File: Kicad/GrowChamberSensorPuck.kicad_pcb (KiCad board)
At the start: 2 copper layers, 11 parts, among them P1 CONN_01X07, U1 Si7006, U2 CCS811

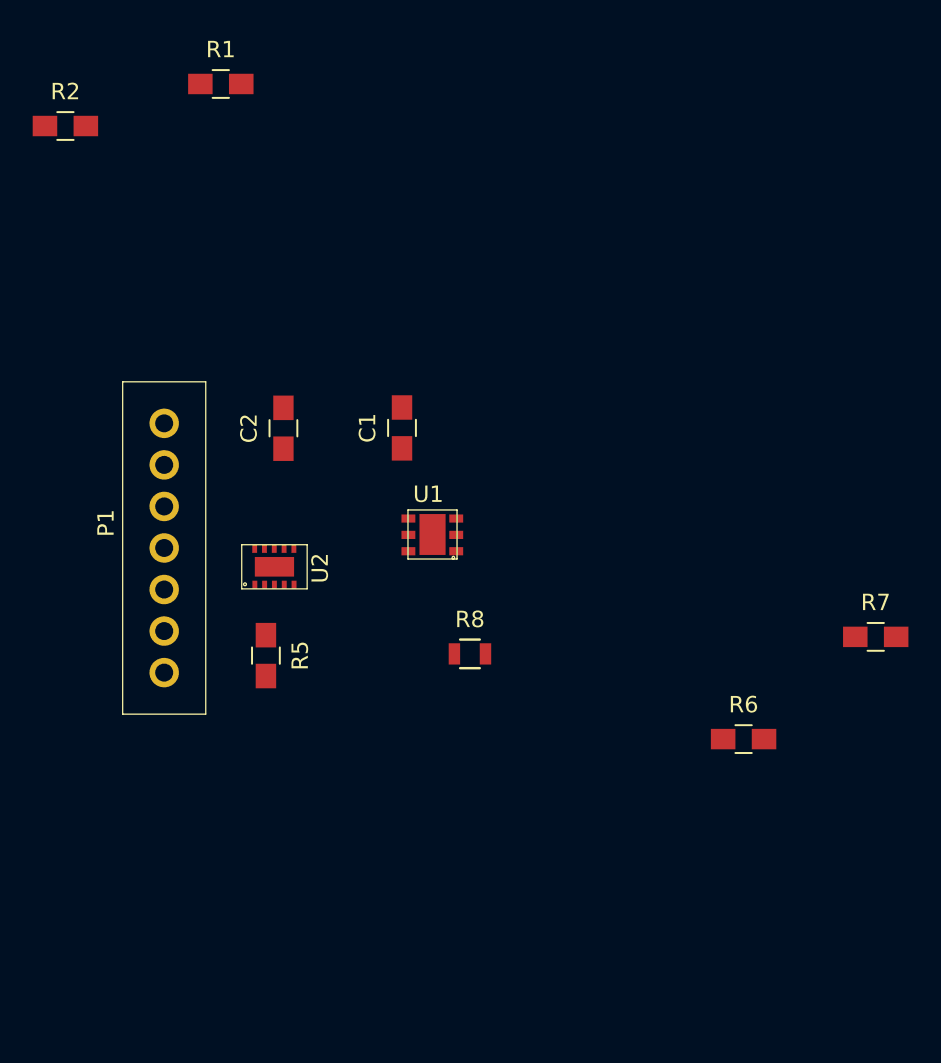
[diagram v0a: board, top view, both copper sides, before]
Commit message: updated GrowChamberSensorPuck Kicad stuff
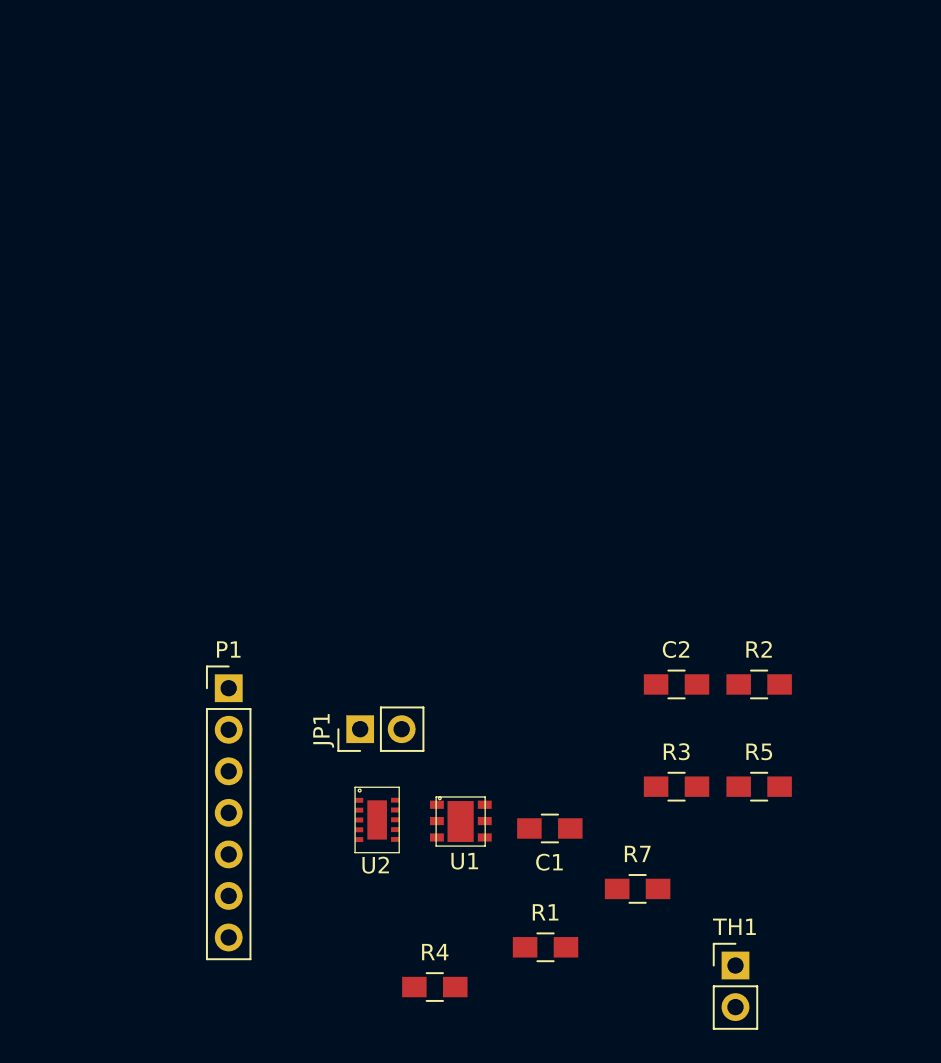
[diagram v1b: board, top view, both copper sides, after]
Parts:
- removed R6: 4K7, Capacitors_SMD:C_0805_HandSoldering
- removed R8: NTC100K, Resistors_SMD:R_0805
- added JP1: JMPR, Socket_Strips:Socket_Strip_Straight_1x02_Pitch2.54mm, F.Cu at (161.6, 120.2)
- added R3: 4K7, Capacitors_SMD:C_0805_HandSoldering, F.Cu at (180.9, 123.7)
- added R4: 100K, Capacitors_SMD:C_0805_HandSoldering, F.Cu at (166.1, 136.0)
- added TH1: Thermistor_NTC, Socket_Strips:Socket_Strip_Straight_1x02_Pitch2.54mm, F.Cu at (184.5, 134.6)
- C2: value 4.7u -> 1u
- P1: footprint TheLeafSpa:7 POS Arduino Header -> Socket_Strips:Socket_Strip_Straight_1x07_Pitch2.54mm
- R1, R2: value 4.7K -> 4K7
- R5: value 4K7 -> 100K
- R7: value 100K -> 10K
- moved R1 56.4 mm to (172.9, 133.5)
- moved R2 54.5 mm to (186.0, 117.5)
- moved R5 31.2 mm to (186.0, 123.7), turned to 0 degrees
- moved C2 28.7 mm to (180.9, 117.5), turned to 0 degrees
- moved C1 26.1 mm to (173.2, 126.3), turned to 180 degrees
- moved R7 21.2 mm to (178.5, 130.0)
- moved U2 19.7 mm to (163.9, 127.8), turned to 0 degrees
- moved U1 16.2 mm to (169.2, 124.8), turned to 0 degrees
- moved P1 4.06 mm to (153.5, 117.7), turned to 0 degrees
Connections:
- net /AUX renamed AUX
- net /NINT renamed NINT
- net /NWAKE renamed NWAKE
- net /PWM renamed NTC_SENSE
- C1 pad 2: GNDD -> Net-(C1-Pad2)
- C2 pad 2: GNDD -> /+3.3v
- P1 pad 1: +3V3 -> NRESET
- P1 pad 4: +3V3 -> SCL
- P1 pad 5: +3V3 -> SDA
- P1 pad 6: GNDD -> +3V3
- P1 pad 7: +3V3 -> GNDD
- R1 pad 2: +3V3 -> SCL
- R2 pad 2: +3V3 -> SDA
- R5 pad 1: /ADDR -> +3V3
- R5 pad 2: GNDD -> ADDR
- U1 pad 1: +3V3 -> SDA
- U1 pad 5: +3V3 -> Net-(C1-Pad2)
- U1 pad 6: +3V3 -> SCL
- U2 pad 1: /ADDR -> ADDR
- U2 pad 10: +3V3 -> SCL
- U2 pad 2: +3V3 -> NRESET
- U2 pad 6: +3V3 -> /+3.3v
- U2 pad 9: +3V3 -> SDA
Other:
- net class Default: clearance 0.2 -> 0.1778; trace_width 0.25 -> 0.254; via_dia 0.6 -> 0.6858; via_drill 0.4 -> 0.3302
- net class PWR added: clearance 0.1778, trace_width 0.6096, via_dia 0.6858, via_drill 0.3302
- rule trace_clearance: 0.2 -> 0.1778
